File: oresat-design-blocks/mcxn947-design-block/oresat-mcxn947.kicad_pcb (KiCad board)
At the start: 4 copper layers, 55 x 62.5 mm, 75 parts, among them J1 BKUP-BATT, J10 Conn_02x20_Odd_Even, J2 USB_C_Receptacle_USB2.0_14P, J3 CAN, J4 TERM, J5 10pin ARM SWD, J6 FTDI-UART-6PIN, J9 Conn_02x20_Odd_Even, SW1 RESET, SW2 ISP(BOOT), U1 MCXN947VKLT, U2 TCAN330, U3 TPS62111RSA, Y1 24 MHz, Y2 32.768 KHz

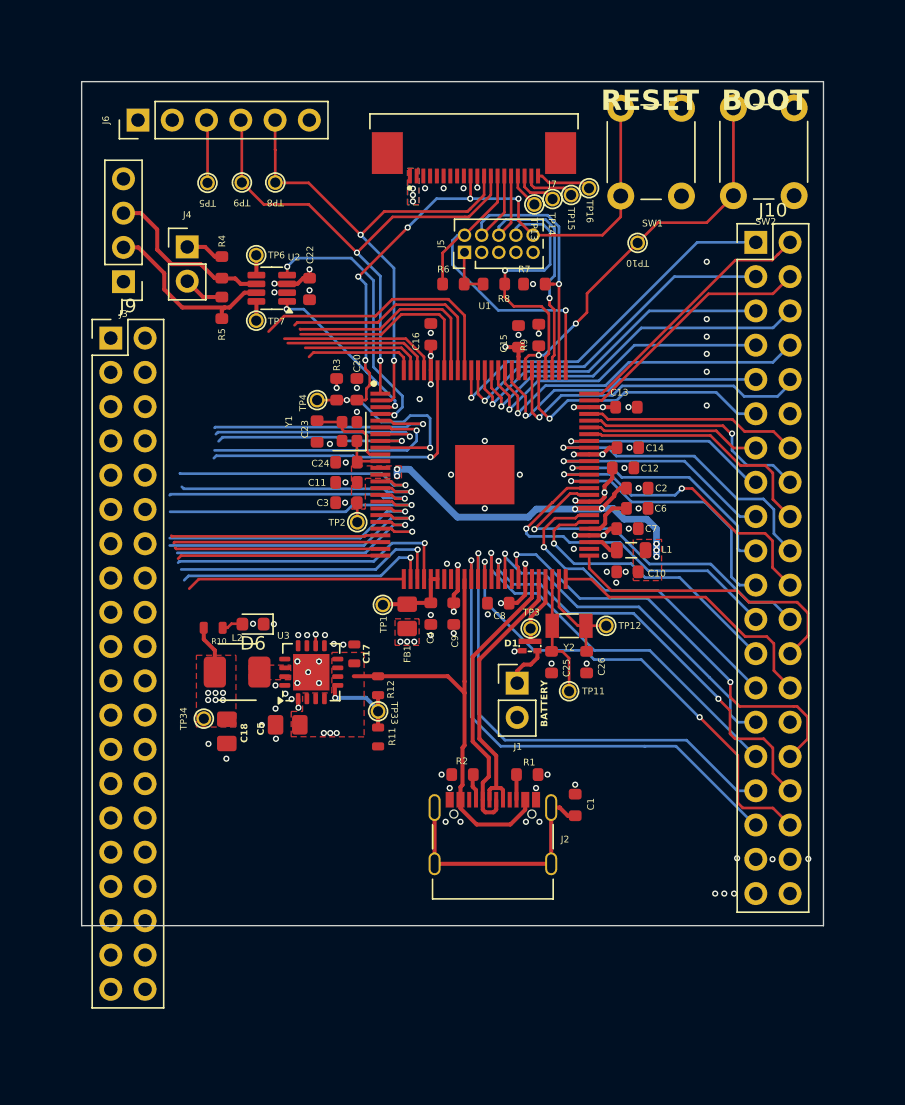
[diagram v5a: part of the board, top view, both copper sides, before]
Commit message: finished initial layout and routing
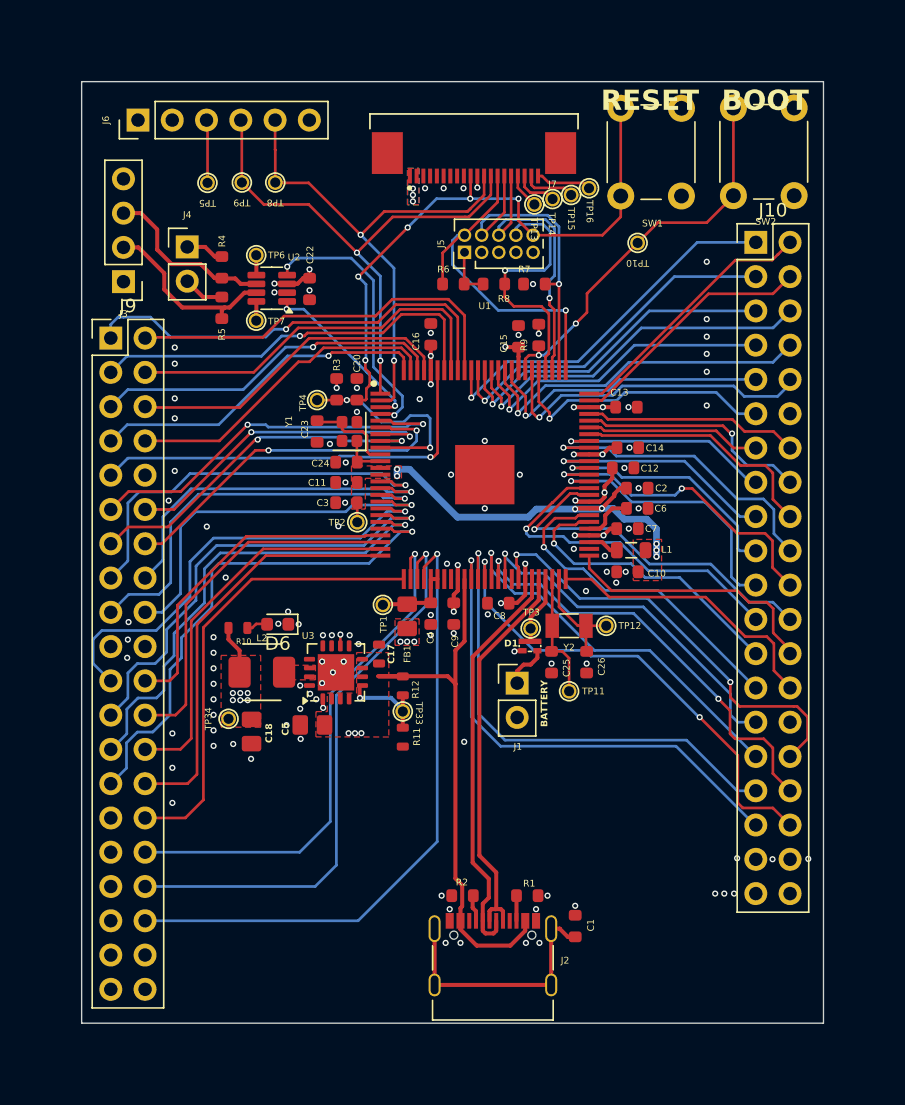
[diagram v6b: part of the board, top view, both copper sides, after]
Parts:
- moved C1 8.98 mm to (167.2, 134.2)
- moved J2 8.98 mm to (161.1, 136.3)
- moved R1 8.98 mm to (163.7, 131.9)
- moved R2 8.98 mm to (158.8, 131.9)
- moved D6 1.83 mm to (145.2, 111.8)
- moved R11 1.83 mm to (154.4, 120.2)
- moved R12 1.83 mm to (154.4, 116.3)
- moved TP33 1.83 mm to (154.4, 118.2)
- moved C17 1.83 mm to (152.7, 114.0)
- moved C18 1.83 mm to (143.2, 119.7)
- moved C5 1.83 mm to (147.7, 119.2)
- moved L2 1.83 mm to (144.0, 115.3)
- moved R10 1.83 mm to (142.2, 112.1)
- moved TP34 1.83 mm to (141.5, 118.8)
- moved U3 1.83 mm to (149.5, 115.4)
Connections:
- J5 pad 2: Net-(J5-SWDIO/TMS) -> SWDIO
- J5 pad 4: Net-(J5-SWCLK/TCK) -> SWCLK
- J5 pad 6: Net-(J5-SWO/TDO) -> SWO
- J6 pad 4: Net-(J6-TXD) -> ISP-UART_TXD
- J6 pad 5: Net-(J6-RXD) -> ISP-UART_RXD
- J9 pad 1: unconnected-(J9-Pin_1-Pad1) -> P1_0
- J9 pad 10: unconnected-(J9-Pin_10-Pad10) -> GND
- J9 pad 11: unconnected-(J9-Pin_11-Pad11) -> P1_12
- J9 pad 12: unconnected-(J9-Pin_12-Pad12) -> P1_14
- J9 pad 13: unconnected-(J9-Pin_13-Pad13) -> P1_15
- J9 pad 14: unconnected-(J9-Pin_14-Pad14) -> P1_13
- J9 pad 15: unconnected-(J9-Pin_15-Pad15) -> Net-(J9-Pin_15)
- J9 pad 16: unconnected-(J9-Pin_16-Pad16) -> Net-(J9-Pin_16)
- J9 pad 17: unconnected-(J9-Pin_17-Pad17) -> Net-(J9-Pin_17)
- J9 pad 18: unconnected-(J9-Pin_18-Pad18) -> Net-(J9-Pin_18)
- J9 pad 19: unconnected-(J9-Pin_19-Pad19) -> GND
- J9 pad 2: unconnected-(J9-Pin_2-Pad2) -> P0_23
- J9 pad 20: unconnected-(J9-Pin_20-Pad20) -> GND
- J9 pad 21: unconnected-(J9-Pin_21-Pad21) -> Net-(J9-Pin_21)
- J9 pad 22: unconnected-(J9-Pin_22-Pad22) -> Net-(J9-Pin_22)
- J9 pad 23: unconnected-(J9-Pin_23-Pad23) -> Net-(J9-Pin_23)
- J9 pad 24: unconnected-(J9-Pin_24-Pad24) -> Net-(J9-Pin_24)
- J9 pad 25: unconnected-(J9-Pin_25-Pad25) -> Net-(J9-Pin_25)
- J9 pad 26: unconnected-(J9-Pin_26-Pad26) -> Net-(J9-Pin_26)
- J9 pad 27: unconnected-(J9-Pin_27-Pad27) -> Net-(J9-Pin_27)
- J9 pad 28: unconnected-(J9-Pin_28-Pad28) -> Net-(J9-Pin_28)
- J9 pad 29: unconnected-(J9-Pin_29-Pad29) -> GND
- J9 pad 3: unconnected-(J9-Pin_3-Pad3) -> P1_2
- J9 pad 30: unconnected-(J9-Pin_30-Pad30) -> Net-(J9-Pin_30)
- J9 pad 31: unconnected-(J9-Pin_31-Pad31) -> GND
- J9 pad 32: unconnected-(J9-Pin_32-Pad32) -> Net-(J9-Pin_32)
- J9 pad 33: unconnected-(J9-Pin_33-Pad33) -> GND
- J9 pad 34: unconnected-(J9-Pin_34-Pad34) -> Net-(J9-Pin_34)
- J9 pad 35: unconnected-(J9-Pin_35-Pad35) -> GND
- J9 pad 36: unconnected-(J9-Pin_36-Pad36) -> Net-(J9-Pin_36)
- J9 pad 37: unconnected-(J9-Pin_37-Pad37) -> GND
- J9 pad 38: unconnected-(J9-Pin_38-Pad38) -> GND
- J9 pad 39: unconnected-(J9-Pin_39-Pad39) -> GND
- J9 pad 4: unconnected-(J9-Pin_4-Pad4) -> P1_1
- J9 pad 40: unconnected-(J9-Pin_40-Pad40) -> GND
- J9 pad 5: unconnected-(J9-Pin_5-Pad5) -> P1_5
- J9 pad 6: unconnected-(J9-Pin_6-Pad6) -> P1_4
- J9 pad 7: unconnected-(J9-Pin_7-Pad7) -> P1_7
- J9 pad 8: unconnected-(J9-Pin_8-Pad8) -> P1_6
- J9 pad 9: unconnected-(J9-Pin_9-Pad9) -> P1_3
- R6 pad 1: Net-(J5-SWDIO/TMS) -> SWDIO
- R7 pad 2: Net-(J5-SWCLK/TCK) -> SWCLK
- TP8 pad 1: Net-(J6-RXD) -> ISP-UART_RXD
- TP9 pad 1: Net-(J6-TXD) -> ISP-UART_TXD
- U1 pad 1: Net-(J6-TXD) -> ISP-UART_TXD
- U1 pad 14: unconnected-(U1D-P2_0-Pad14) -> Net-(J9-Pin_15)
- U1 pad 15: unconnected-(U1D-P2_1-Pad15) -> Net-(J9-Pin_16)
- U1 pad 16: unconnected-(U1D-P2_2-Pad16) -> Net-(J9-Pin_17)
- U1 pad 17: unconnected-(U1D-P2_3-Pad17) -> Net-(J9-Pin_18)
- U1 pad 18: unconnected-(U1D-P2_4-Pad18) -> Net-(J9-Pin_21)
- U1 pad 19: unconnected-(U1D-P2_5-Pad19) -> Net-(J9-Pin_23)
- U1 pad 2: Net-(J6-RXD) -> ISP-UART_RXD
- U1 pad 20: unconnected-(U1D-P2_6-Pad20) -> Net-(J9-Pin_25)
- U1 pad 21: unconnected-(U1D-P2_7-Pad21) -> Net-(J9-Pin_27)
- U1 pad 22: unconnected-(U1F-P4_0/ANA_0-Pad22) -> Net-(J9-Pin_22)
- U1 pad 23: unconnected-(U1F-P4_1/ANA_1-Pad23) -> Net-(J9-Pin_24)
- U1 pad 24: unconnected-(U1F-P4_2-Pad24) -> Net-(J9-Pin_26)
- U1 pad 25: unconnected-(U1F-P4_3-Pad25) -> Net-(J9-Pin_28)
- U1 pad 26: unconnected-(U1F-P4_4/ANA_4-Pad26) -> Net-(J9-Pin_30)
- U1 pad 27: unconnected-(U1F-P4_5/ANA_5-Pad27) -> Net-(J9-Pin_32)
- U1 pad 28: unconnected-(U1F-P4_6/ANA_6-Pad28) -> Net-(J9-Pin_34)
- U1 pad 29: unconnected-(U1F-P4_7/ANA_7-Pad29) -> Net-(J9-Pin_36)
- U1 pad 76: Net-(J5-SWDIO/TMS) -> SWDIO
- U1 pad 77: Net-(J5-SWCLK/TCK) -> SWCLK
- U1 pad 78: Net-(J5-SWO/TDO) -> SWO
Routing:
- net Net-(J9-Pin_36): track 0.00 -> 47.7 mm, vias 0 -> 1
- net Net-(J9-Pin_34): track 0.00 -> 42.8 mm, vias 0 -> 1
- net Net-(J9-Pin_32): track 0.00 -> 39.1 mm, vias 0 -> 1
- net Net-(J9-Pin_27): track 0.00 -> 38.1 mm, vias 0 -> 1
- net ISP-UART_RXD: track 2.86 -> 38.5 mm, vias 0 -> 2
- net Net-(J6-RXD): track 35.6 -> 0.00 mm, vias 2 -> 0
- net Net-(J9-Pin_25): track 0.00 -> 35.2 mm, vias 0 -> 1
- net Net-(J9-Pin_23): track 0.00 -> 34.3 mm, vias 0 -> 1
- net Net-(J9-Pin_21): track 0.00 -> 34.1 mm, vias 0 -> 1
- net Net-(J9-Pin_30): track 0.00 -> 34.0 mm
- net Net-(J9-Pin_28): track 0.00 -> 30.9 mm
- net Net-(J9-Pin_17): track 0.00 -> 30.1 mm, vias 0 -> 1
- net Net-(J9-Pin_15): track 0.00 -> 29.9 mm, vias 0 -> 1
- net Net-(J9-Pin_26): track 0.00 -> 28.7 mm
- net Net-(J9-Pin_18): track 0.00 -> 28.4 mm, vias 0 -> 1
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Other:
- board size 55 x 62.5 mm -> 55 x 69.8 mm

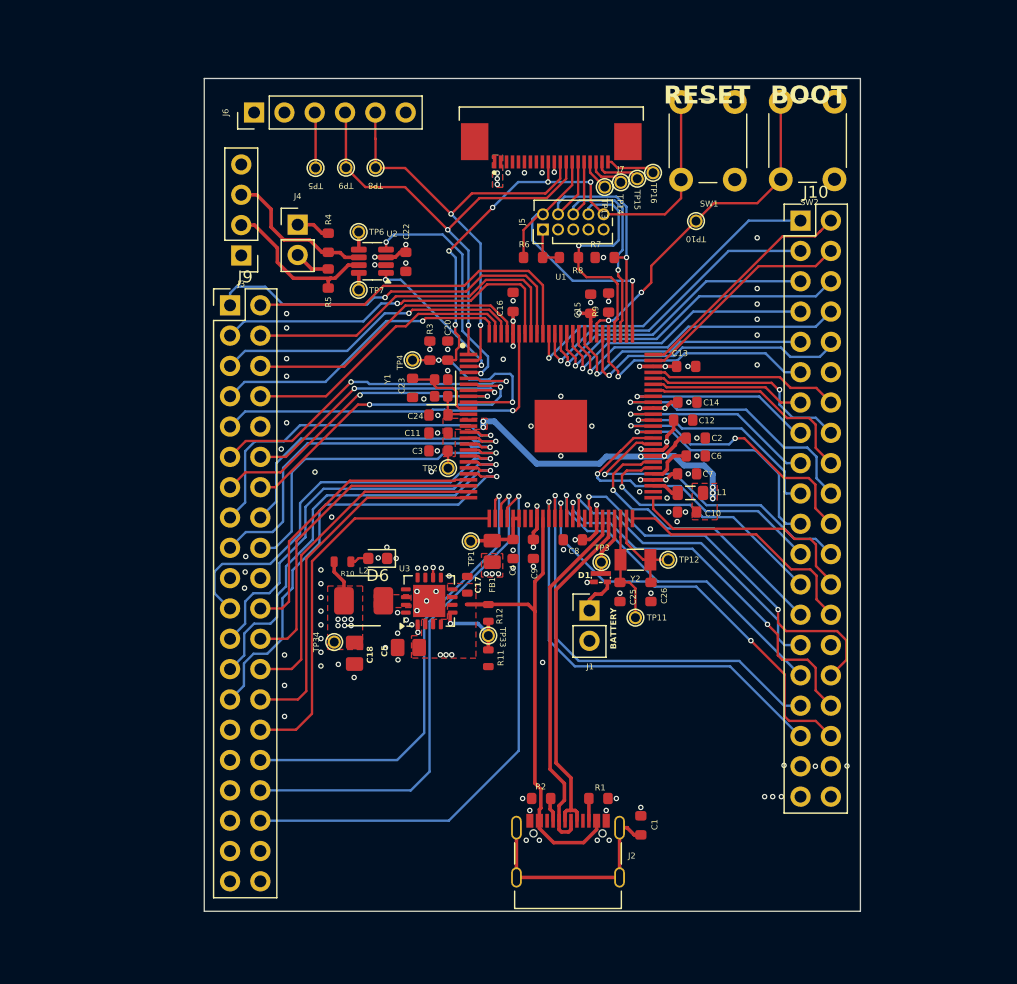
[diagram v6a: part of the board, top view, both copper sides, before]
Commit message: Final revision after design review. Added labels for all breakout pins and cleaned up silkscreen.
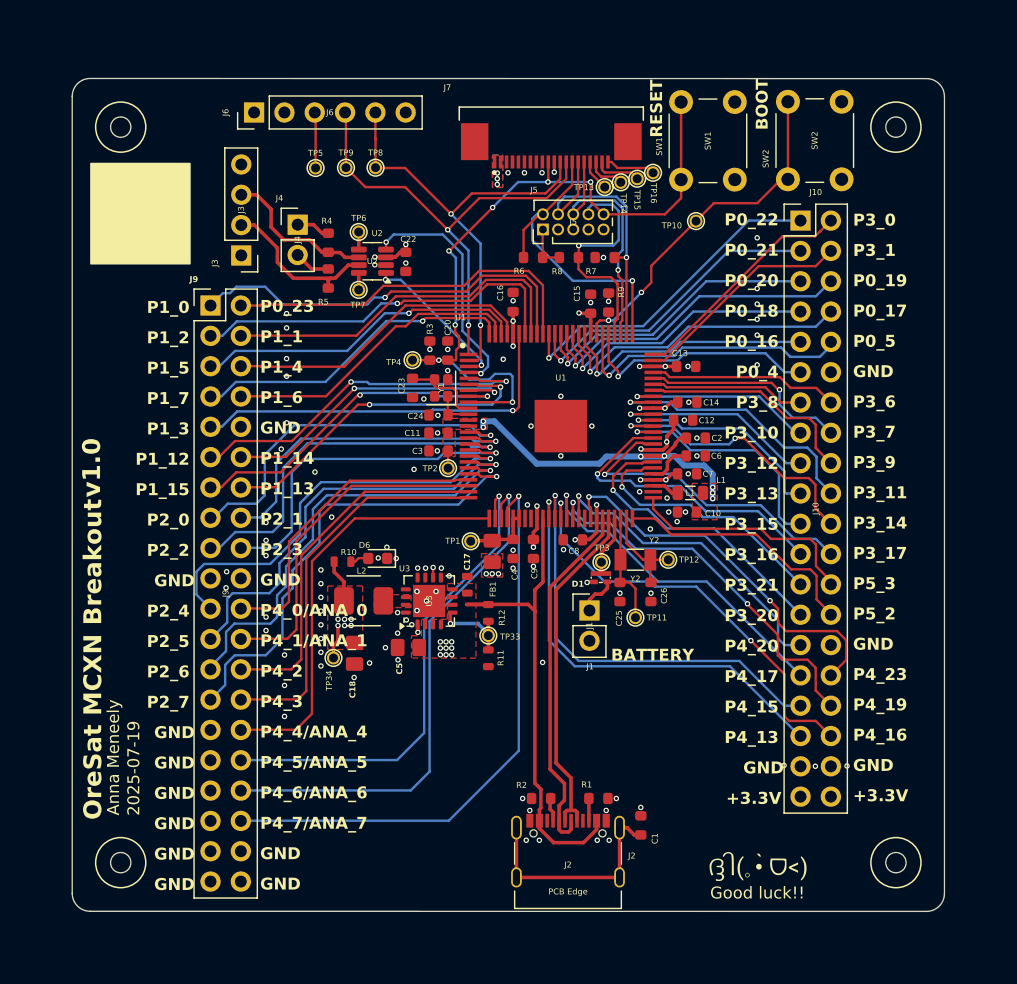
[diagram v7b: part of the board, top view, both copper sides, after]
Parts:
- added G***: LOGO, LOGO, F.Cu at (176.9, 137.7)
- added HW1: M1.6_Mounting_Hole, oresat-misc:M1.6 Mounting Hole, F.Cu at (188.6, 75.7)
- added HW2: M1.6_Mounting_Hole, oresat-misc:M1.6 Mounting Hole, F.Cu at (123.6, 75.7)
- added HW3: M1.6_Mounting_Hole, oresat-misc:M1.6 Mounting Hole, F.Cu at (188.6, 137.3)
- added HW4: M1.6_Mounting_Hole, oresat-misc:M1.6 Mounting Hole, F.Cu at (123.6, 137.3)
- moved J9 1.64 mm to (131.2, 90.6)
- moved TP34 1.33 mm to (141.4, 120.1)
- moved SW2 0.60 mm to (184.0, 73.5)
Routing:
- net +3.3V: track 59.6 -> 57.9 mm, vias 34 -> 31
- net Net-(J9-Pin_23): track 34.3 -> 36.0 mm
- net Net-(J9-Pin_25): track 35.2 -> 36.9 mm
- net P1_3: track 31.1 -> 32.7 mm
- net P1_5: track 26.1 -> 27.7 mm
- net P1_13: track 26.8 -> 28.5 mm
- net P1_15: track 26.5 -> 28.2 mm
- net P0_23: track 29.4 -> 31.1 mm
- net Net-(J9-Pin_26): track 28.7 -> 30.3 mm
- net Net-(J9-Pin_24): track 27.1 -> 28.7 mm
- net Net-(J9-Pin_17): track 30.1 -> 31.8 mm
- net Net-(J9-Pin_36): track 47.7 -> 49.3 mm
- net Net-(J9-Pin_34): track 42.8 -> 44.4 mm
- net Net-(J9-Pin_30): track 34.0 -> 35.6 mm
- net Net-(J9-Pin_28): track 30.9 -> 32.6 mm
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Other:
- board size 55 x 69.8 mm -> 73.1 x 69.8 mm
- board text added: "${ISSUE_DATE}"
- board text added: "+3.3V"
- board text added: "Anna Meneely"
- board text added: "GND"
- board text added: "Good luck!!"
- board text added: "OreSat MCXN Breakout"
- board text added: "P0_16"
- board text added: "P0_17"
- board text added: "P0_18"
- board text added: "P0_19"
- board text added: "P0_20"
- board text added: "P0_21"
- board text added: "P0_22"
- board text added: "P0_23"
- board text added: "P0_4"
- board text added: "P0_5"
- board text added: "P1_0"
- board text added: "P1_1"
- board text added: "P1_12"
- board text added: "P1_13"
- board text added: "P1_14"
- board text added: "P1_15"
- board text added: "P1_2"
- board text added: "P1_3"
- board text added: "P1_4"
- board text added: "P1_5"
- board text added: "P1_6"
- board text added: "P1_7"
- board text added: "P2_0"
- board text added: "P2_1"
- board text added: "P2_2"
- board text added: "P2_3"
- board text added: "P2_4"
- board text added: "P2_5"
- board text added: "P2_6"
- board text added: "P2_7"
- board text added: "P3_0"
- board text added: "P3_1"
- board text added: "P3_10"
- board text added: "P3_11"
- board text added: "P3_12"
- board text added: "P3_13"
- board text added: "P3_14"
- board text added: "P3_15"
- board text added: "P3_16"
- board text added: "P3_17"
- board text added: "P3_20"
- board text added: "P3_21"
- board text added: "P3_6"
- board text added: "P3_7"
- board text added: "P3_8"
- board text added: "P3_9"
- board text added: "P4_0/ANA_0"
- board text added: "P4_1/ANA_1"
- board text added: "P4_13"
- board text added: "P4_15"
- board text added: "P4_16"
- board text added: "P4_17"
- board text added: "P4_19"
- board text added: "P4_2"
- board text added: "P4_20"
- board text added: "P4_23"
- board text added: "P4_3"
- board text added: "P4_4/ANA_4"
- board text added: "P4_5/ANA_5"
- board text added: "P4_6/ANA_6"
- board text added: "P4_7/ANA_7"
- board text added: "P5_2"
- board text added: "P5_3"
- board text added: "v${REVISION}"

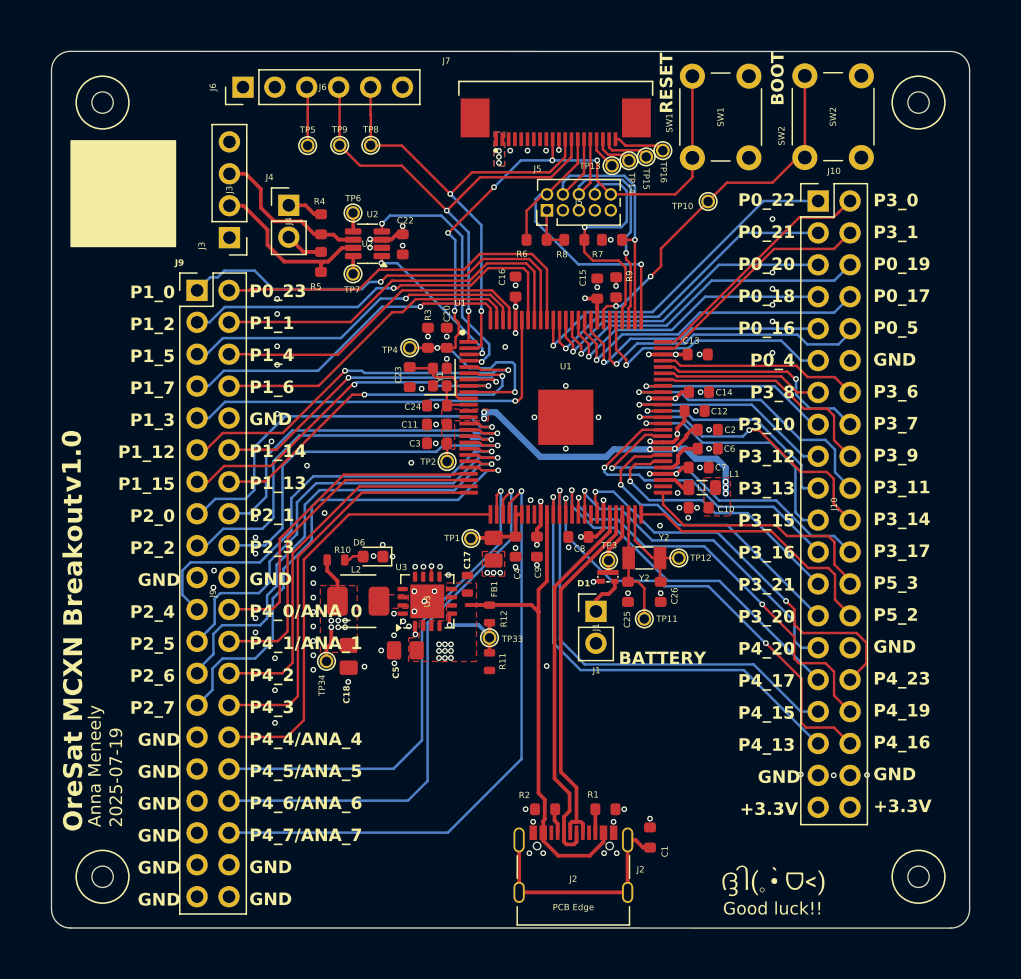
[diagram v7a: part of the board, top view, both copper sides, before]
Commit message: Some ERC checking and fixing, and then dep dive into oresat passive library. Sorry Anna. Go fix all the silkscreen.
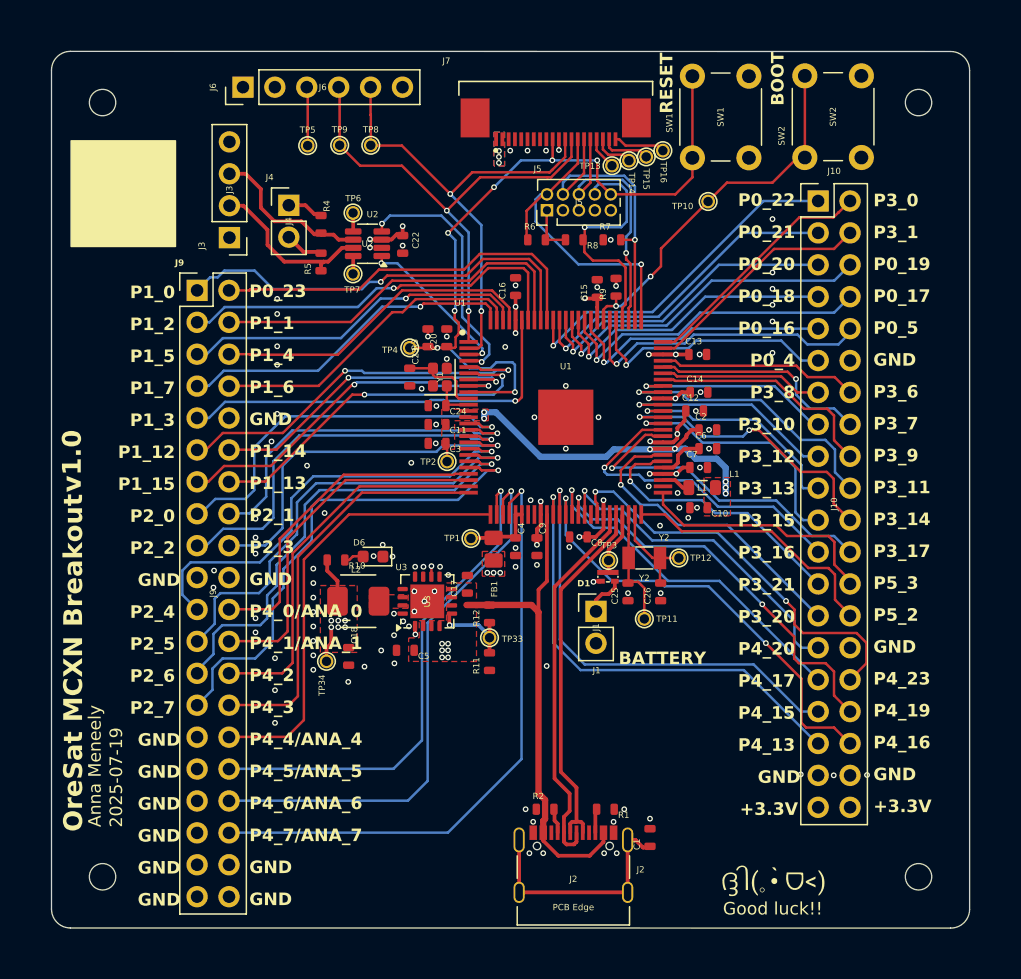
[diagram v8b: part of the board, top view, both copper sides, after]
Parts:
- C1, C10, C11, C12, C13, C14, C15, C16, C2, C20, C22, C23, C24, C25, C26, C3, C4, C6, C7, C8, C9, R1, R2, R3, R4, R5, R6, R7, R8, R9: footprint oresat-passives:0603-B-NOSILK -> oresat-passives:0603-C-NOSILK
- C18, C5: footprint oresat-passives:0805-B-NOSILK -> oresat-passives:0603-C-NOSILK
- HW1, HW2, HW3, HW4: value M1.6_Mounting_Hole -> M2 Mounting Hole; footprint oresat-misc:M1.6 Mounting Hole -> oresat-misc:Hole-2.1mm-NPTH
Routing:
- net VBUS: vias 12 -> 9
